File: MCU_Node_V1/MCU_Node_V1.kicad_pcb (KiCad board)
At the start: 2 copper layers, 90.2 x 48.8 mm, 97 parts, among them J1 Conn_01x02_Socket, J10 Conn_01x02_Socket, J11 USB_B_Micro, J12 POWER_SELECT, J13 Conn_01x02_Socket, J14 Conn_01x02_Socket, J15 Conn_01x02_Socket, J16 Conn_01x02_Socket, J17 Conn_01x02_Socket, J18 Conn_01x02_Socket, J19 Timer Config, J2 DC_IN, J3 Conn_01x03_Socket, J4 REG_CTRL, J6 Conn_01x10, J7 Conn_01x02, J8 Conn_01x02, J9 REG_EN, Q1 BSS138, Q4 BSS138, SW1 SW_Push, SW2 SW_Push, SW4 LPM_RST, U1 74HC595, U2 CH340C, U3 MIKROE, U4 TPS73733DCQR, U5 ESP32-WROOM-32, U8 TPL5110

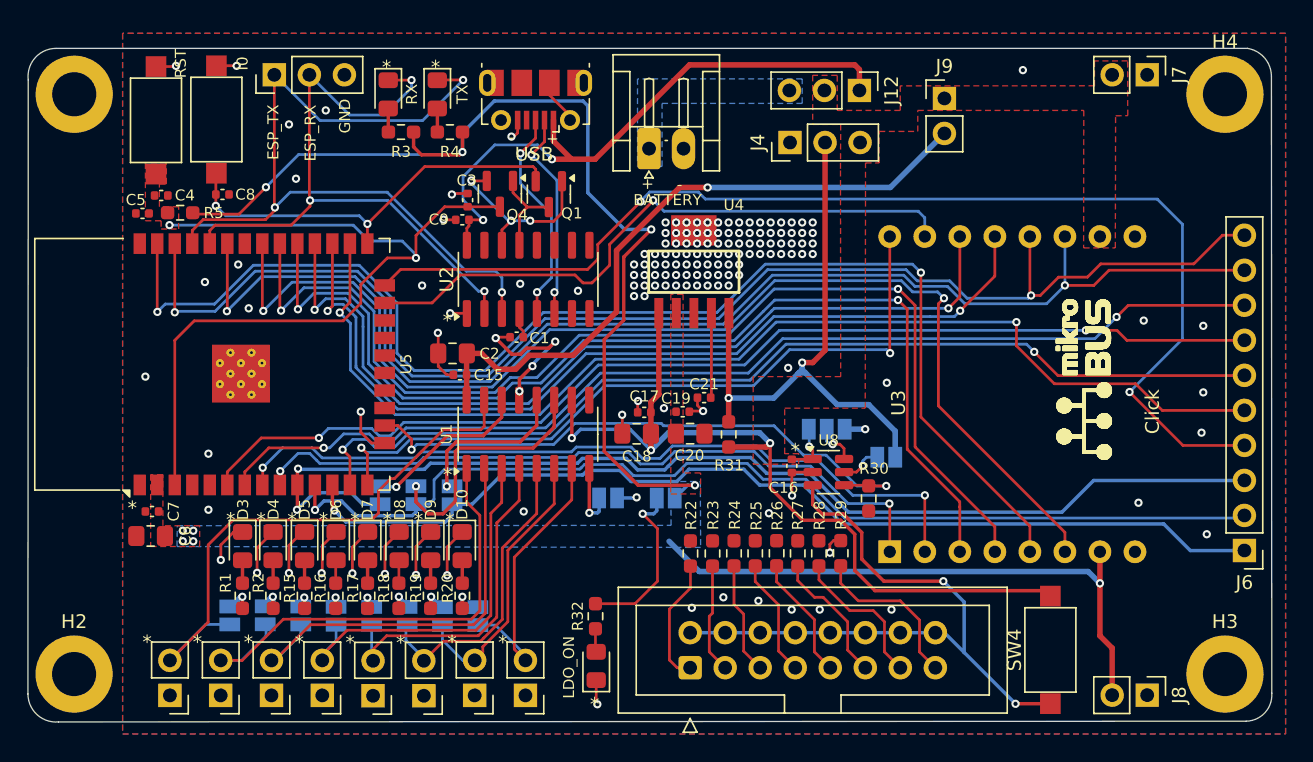
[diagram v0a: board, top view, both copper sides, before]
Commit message: 98 percent
-drc warning negliglble
-additional designation thru silkscreen for the timer and led ports
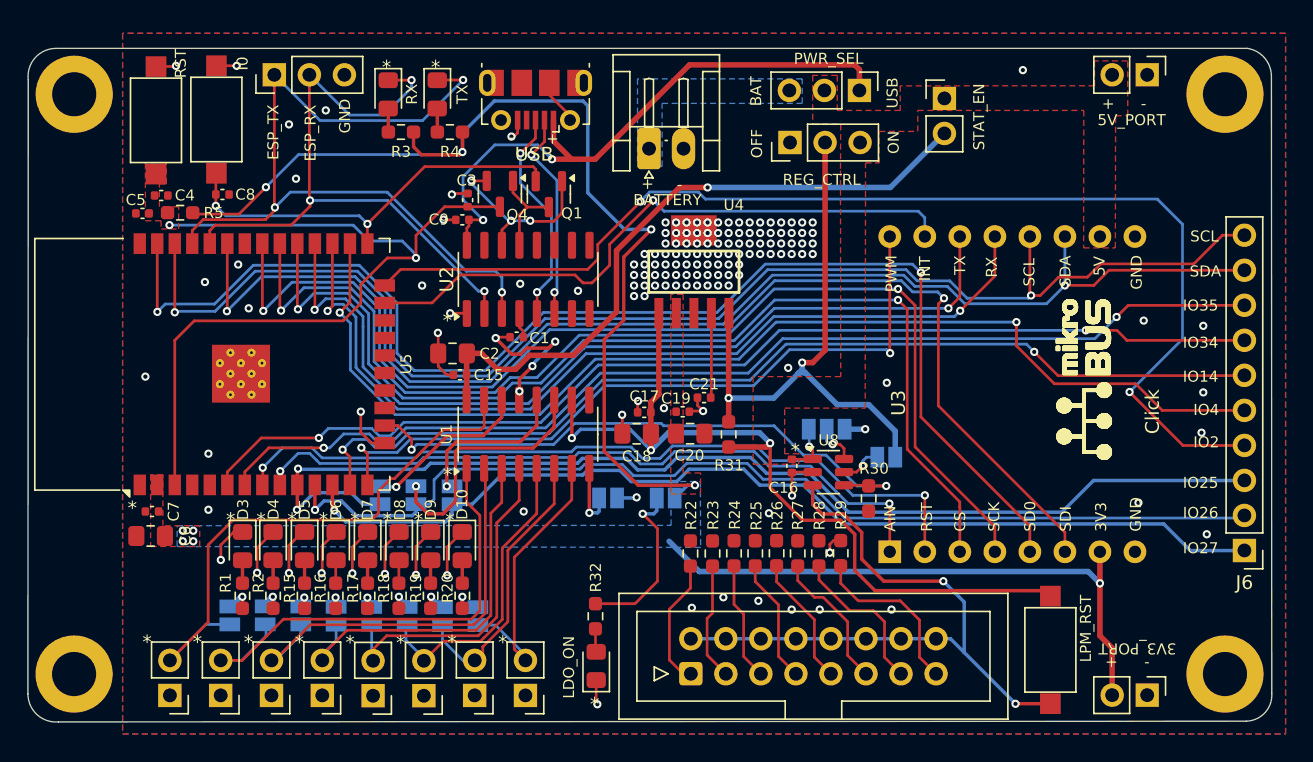
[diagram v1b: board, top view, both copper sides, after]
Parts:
- moved J19 0.44 mm to (214.4, 96.7)
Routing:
- net Net-(J19-Pin_3): track 7.94 -> 8.53 mm
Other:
- board text added: "3V3"
- board text added: "5V"
- board text added: "AIN"
- board text added: "BAT"
- board text added: "CS"
- board text added: "INT"
- board text added: "IO14"
- board text added: "IO2"
- board text added: "IO25"
- board text added: "IO26"
- board text added: "IO27"
- board text added: "IO34"
- board text added: "IO35"
- board text added: "IO4"
- board text added: "OFF"
- board text added: "ON"
- board text added: "PWM"
- board text added: "RST"
- board text added: "RX"
- board text added: "SCK"
- board text added: "SCL"
- board text added: "SD0"
- board text added: "SDA"
- board text added: "SDI"
- board text added: "TX"
- board text added: "USB"

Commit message: done
-to be approve
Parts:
- moved JP17 2.64 mm to (230.3, 79.0)
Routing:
- net Net-(JP17-B): track 3.06 -> 6.19 mm
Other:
- board text added: "1hr"
- board text added: "1min"
- board text added: "20mins"
- board text added: "2hrs"
- board text added: "30mins"
- board text added: "30s"
- board text added: "3mins"
- board text added: "5mins"
- board text added: "D10_EN"
- board text added: "D3_EN"
- board text added: "D4_EN"
- board text added: "D5_EN"
- board text added: "D6_EN"
- board text added: "D7_EN"
- board text added: "D8_EN"
- board text added: "D9_EN"
- board text added: "QA"
- board text added: "QB"
- board text added: "QC"
- board text added: "QD"
- board text added: "QE"
- board text added: "QF"
- board text added: "QG"
- board text added: "QH"
- board text added: "STAT_PORT"
- board text added: "TIMER CONFIG"
- board text added: "VCC"
